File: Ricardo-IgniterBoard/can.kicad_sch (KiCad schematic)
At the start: 9 parts, among them U2 SN65HVD230

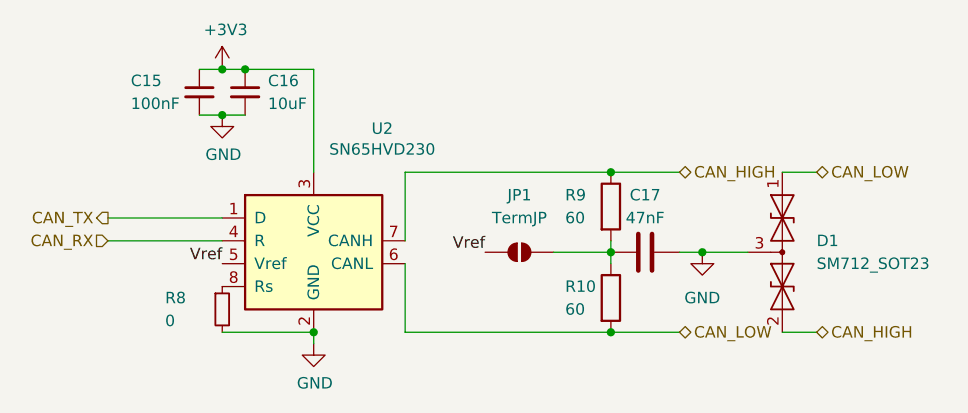
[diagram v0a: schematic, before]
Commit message: Assigning components
And added the thermocouple
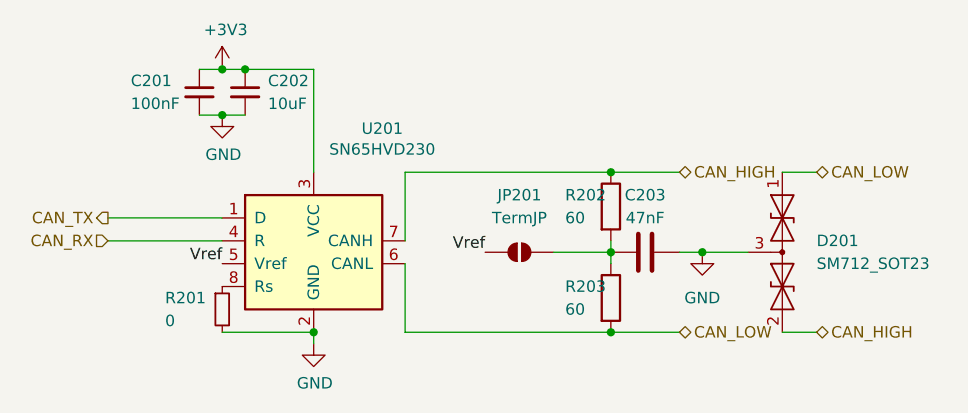
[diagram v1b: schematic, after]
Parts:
- renumbered C15 to C201, C16 to C202, C17 to C203, D1 to D201, JP1 to JP201, R8 to R201, R9 to R202, R10 to R203, U2 to U201
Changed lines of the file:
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@@
 		(dnp no)
 		(fields_autoplaced yes)
-		(property "Reference" "U2"
+		(property "Reference" "U201"
 			(at 142.24 75.1586 0)
 			(effects
@@
 			(project "RicardoTemplate"
 				(path "/7db990e4-92e1-4f99-b4d2-435bbec1ba83/00000000-0000-0000-0000-000061942b9a"
-					(reference "U2")
+					(reference "U201")
 					(unit 1)
 				)
@@
 		(dnp no)
 		(fields_autoplaced yes)
-		(property "Reference" "C16"
+		(property "Reference" "C202"
 			(at 129.54 69.8562 0)
 			(effects
@@
 			(project "RicardoTemplate"
 				(path "/7db990e4-92e1-4f99-b4d2-435bbec1ba83/00000000-0000-0000-0000-000061942b9a"
-					(reference "C16")
+					(reference "C202")
 					(unit 1)
 				)
@@
 		(dnp no)
 		(fields_autoplaced yes)
-		(property "Reference" "D1"
+		(property "Reference" "D201"
 			(at 190.5 87.63 90)
 			(effects
@@
 			(project "RicardoTemplate"
 				(path "/7db990e4-92e1-4f99-b4d2-435bbec1ba83/00000000-0000-0000-0000-000061942b9a"
-					(reference "D1")
+					(reference "D201")
 					(unit 1)
 				)
@@
 		(dnp no)
 		(fields_autoplaced yes)
-		(property "Reference" "C15"
+		(property "Reference" "C201"
 			(at 114.3 69.85 0)
 			(effects
@@
 			(project "RicardoTemplate"
 				(path "/7db990e4-92e1-4f99-b4d2-435bbec1ba83/00000000-0000-0000-0000-000061942b9a"
-					(reference "C15")
+					(reference "C201")
 					(unit 1)
 				)
@@
 		(on_board yes)
 		(dnp no)
-		(property "Reference" "R8"
+		(property "Reference" "R201"
 			(at 118.11 93.98 0)
 			(effects
@@
 			(project "RicardoTemplate"
 				(path "/7db990e4-92e1-4f99-b4d2-435bbec1ba83/00000000-0000-0000-0000-000061942b9a"
-					(reference "R8")
+					(reference "R201")
 					(unit 1)
 				)
@@
 		(dnp no)
 		(fields_autoplaced yes)
-		(property "Reference" "R10"
+		(property "Reference" "R203"
 			(at 162.56 92.71 0)
 			(effects
@@
 			(project "RicardoTemplate"
 				(path "/7db990e4-92e1-4f99-b4d2-435bbec1ba83/00000000-0000-0000-0000-000061942b9a"
-					(reference "R10")
+					(reference "R203")
 					(unit 1)
 				)
@@
 		(dnp no)
 		(fields_autoplaced yes)
-		(property "Reference" "R9"
+		(property "Reference" "R202"
 			(at 162.56 82.55 0)
 			(effects
@@
 			(project "RicardoTemplate"
 				(path "/7db990e4-92e1-4f99-b4d2-435bbec1ba83/00000000-0000-0000-0000-000061942b9a"
-					(reference "R9")
+					(reference "R202")
 					(unit 1)
 				)
@@
 		(dnp no)
 		(fields_autoplaced yes)
-		(property "Reference" "C17"
+		(property "Reference" "C203"
 			(at 171.45 82.55 90)
 			(effects
@@
 			(project "RicardoTemplate"
 				(path "/7db990e4-92e1-4f99-b4d2-435bbec1ba83/00000000-0000-0000-0000-000061942b9a"
-					(reference "C17")
+					(reference "C203")
 					(unit 1)
 				)
@@
 		(dnp no)
 		(fields_autoplaced yes)
-		(property "Reference" "JP1"
+		(property "Reference" "JP201"
 			(at 157.48 82.55 0)
 			(effects
@@
 			(project "RicardoTemplate"
 				(path "/7db990e4-92e1-4f99-b4d2-435bbec1ba83/00000000-0000-0000-0000-000061942b9a"
-					(reference "JP1")
-					(unit 1)
-				)
+					(reference "JP201")
+					(unit 1)
+				)
